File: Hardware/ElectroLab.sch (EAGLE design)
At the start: 244 parts, among them IC1 LM2902DT, IC10 CD4511BNSR, IC11 PAM8403, IC12 LM2902DT, IC13 ADXL337, IC14 MIC5205, IC2 LM2902DT, IC3 SN74LV08ADR, IC4 SN74LV32ADR, IC5 SN74LV04ADR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

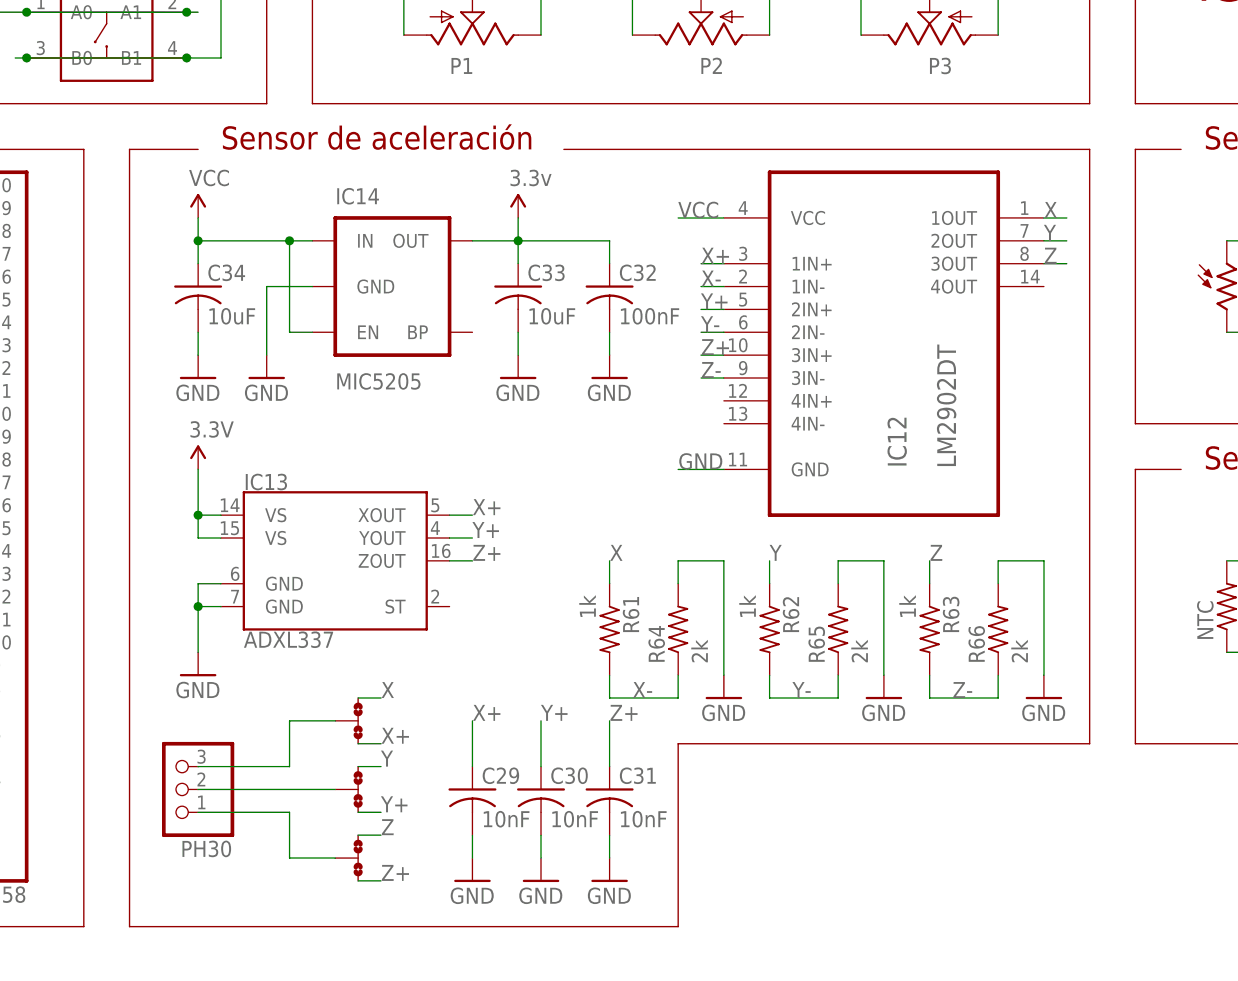
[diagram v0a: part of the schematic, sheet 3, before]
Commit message: Removed Amplifier after Acc ADXL337
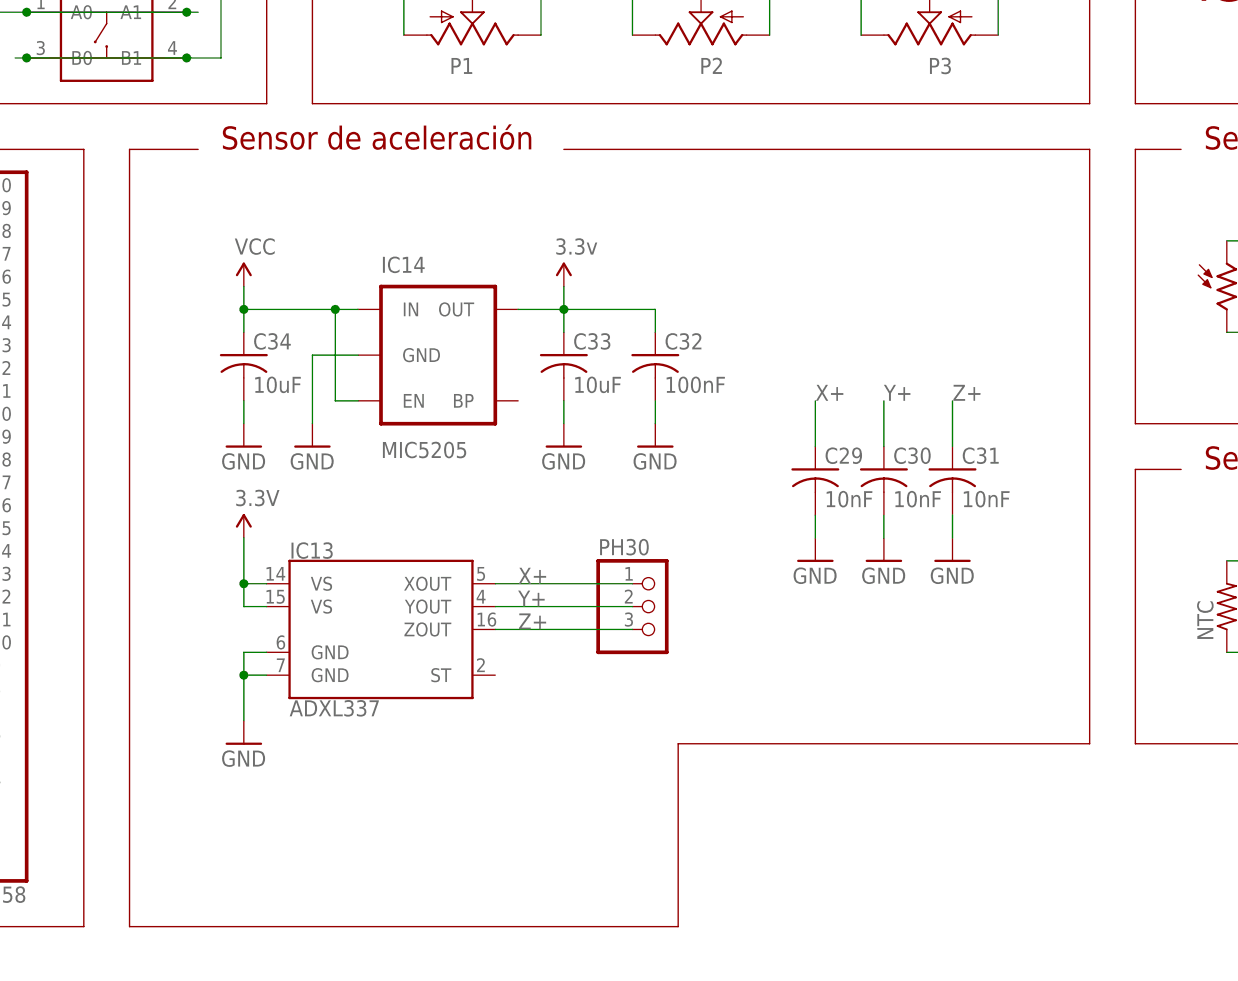
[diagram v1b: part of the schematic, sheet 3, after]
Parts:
- removed IC12: LM2902DT, Texas Instruments_By_element14_Batch_1:LM2902DT
- removed JMP7, JMP8, JMP9: 0R-JUMPA, jump-0r-smd:0R-JUMPA
- removed R61, R62, R63: 1k, SpaceDIY_passive_components:R0603
- removed R64, R65, R66: 2k, SpaceDIY_passive_components:R0603
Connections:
- removed net N$124: JMP8-0R.2, PH30.2
- removed net N$127: JMP7-0R.2, PH30.3
- removed net N$128: JMP9-0R.2, PH30.1
- removed net X: IC12.1OUT, JMP7-0R.3, R61.1
- removed net X-: IC12.1IN-, R61.2, R64.1
- removed net Y: IC12.2OUT, JMP8-0R.3, R62.1
- removed net Y-: IC12.2IN-, R62.2, R65.1
- removed net Z: IC12.3OUT, JMP9-0R.3, R63.1
- removed net Z-: IC12.3IN-, R63.2, R66.1
- net GND: no longer IC12.GND, R64.2, R65.2, R66.2
- net VCC: no longer IC12.VCC
- net X+: now also PH30.1; no longer IC12.1IN+, JMP7-0R.1
- net Y+: now also PH30.2; no longer IC12.2IN+, JMP8-0R.1
- net Z+: now also PH30.3; no longer IC12.3IN+, JMP9-0R.1
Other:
- moved on the sheet: C29, C30, C31, C32, C33, C34, IC13, IC14, PH30

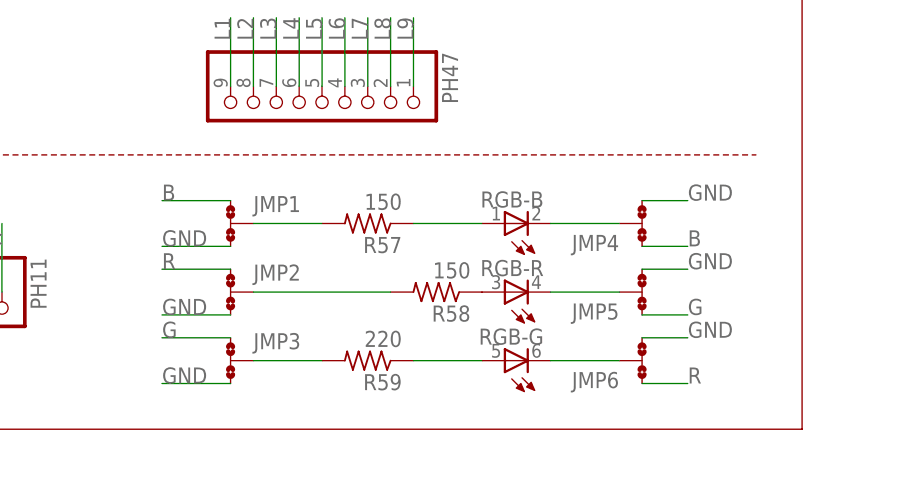
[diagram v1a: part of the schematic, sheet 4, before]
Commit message: Updated RGB layout
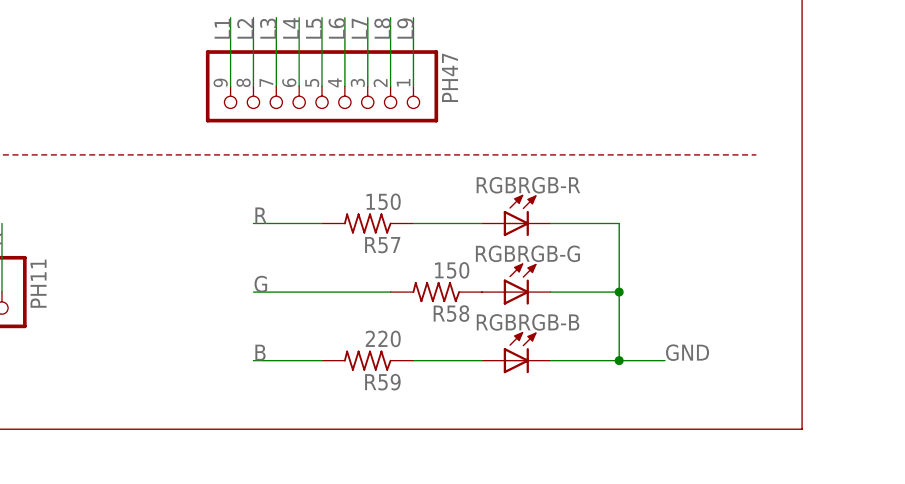
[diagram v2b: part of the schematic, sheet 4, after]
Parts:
- removed JMP1, JMP2, JMP3, JMP4, JMP5, JMP6: 0R-JUMPA, jump-0r-smd:0R-JUMPA
- RGB: value OVSTRGBBCR8 -> LED_RGB_PLCC6; device led:OVSTRGBBCR8 -> Passive_components:LED_RGB_PLCC6
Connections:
- removed net N$118: JMP2.2, R58.2
- removed net N$119: JMP3.2, R59.2
- removed net N$120: JMP4.2, RGB-B.C
- removed net N$121: JMP5.2, RGB-R.C
- removed net N$122: JMP6.2, RGB-G.C
- removed net N$309: R58.1, RGB-R.A
- net B: now also R59.2; no longer JMP1.1, JMP4.1
- net G: now also R58.2; no longer JMP3.1, JMP5.1
- net GND: now also RGBRGB-B.C, RGBRGB-G.C, RGBRGB-R.C; no longer JMP1.3, JMP2.3, JMP3.3, JMP4.3, JMP5.3, JMP6.3
- net N$117: now also R58.1, RGBRGB-G.A; no longer JMP1.2, R57.2
- net N$308: now also RGBRGB-R.A; no longer RGB-B.A
- net N$310: now also RGBRGB-B.A; no longer RGB-G.A
- net R: now also R57.2; no longer JMP2.1, JMP6.1

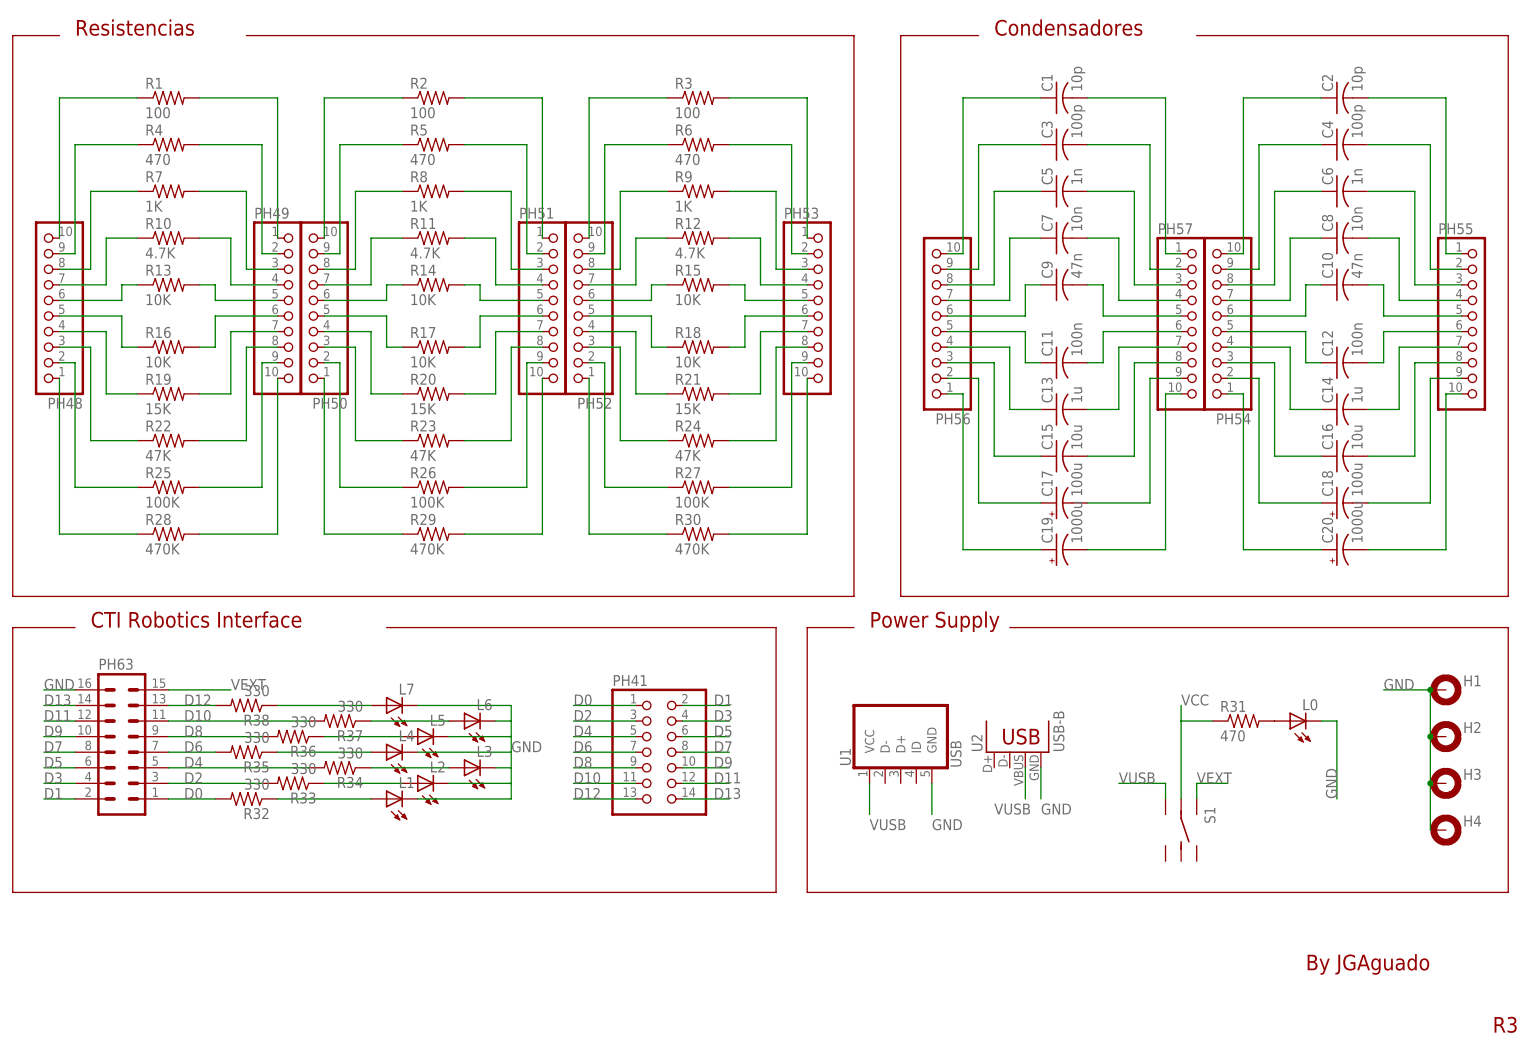
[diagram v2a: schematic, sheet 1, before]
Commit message: Capacitor area update: - Replaced C19 & C20 for 470uF 7343 (2917) Tantalum capacitors - Added C35 & C36 470uF 7343 (2917) in paralel to C19 & C20 for making 940uF combined - Reviewed Name and Values silkscreen for capacitors
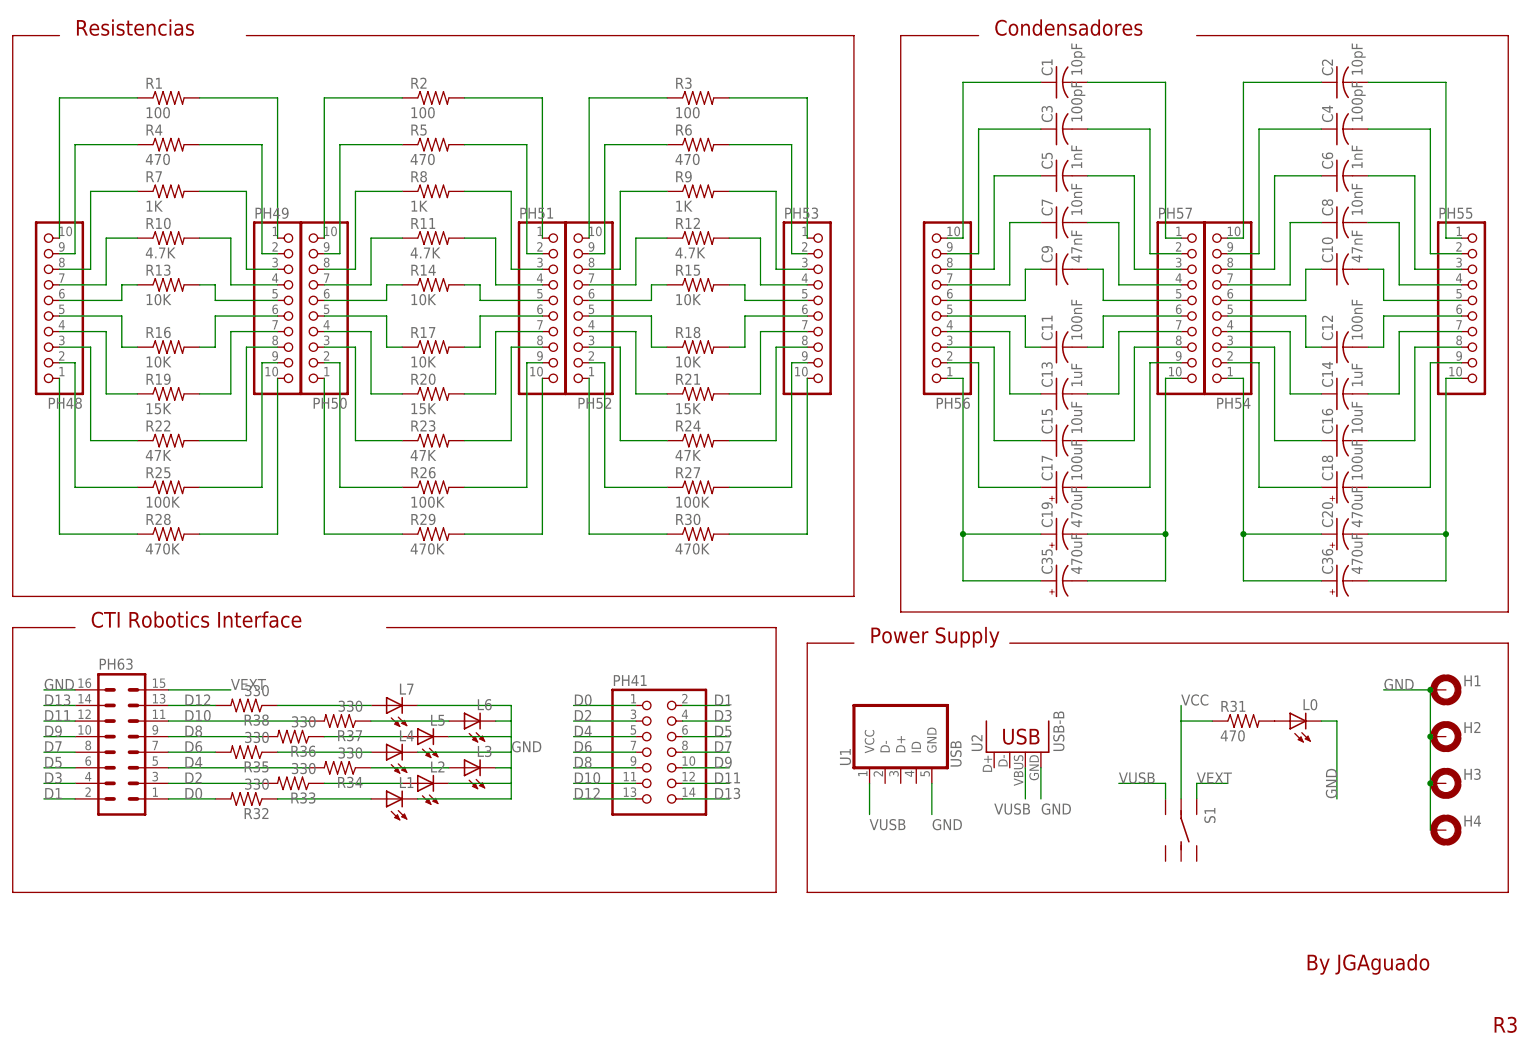
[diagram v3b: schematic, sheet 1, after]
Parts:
- added C35, C36: 470uF, rcl:CPOL-USD/7343-31R
- C1, C2: value 10p -> 10pF
- C10, C9: value 47n -> 47nF
- C11, C12: value 100n -> 100nF
- C13, C14: value 1u -> 1uF
- C15, C16: value 10u -> 10uF
- C17, C18: value 100u -> 100uF; device rcl:CPOL-USA/3216-18W -> rcl:CPOL-USA/3216-18R
- C19, C20: value 1000u -> 470uF; device rcl:CPOL-USD/7343-31W -> rcl:CPOL-USD/7343-31R
- C3, C4: value 100p -> 100pF
- C5, C6: value 1n -> 1nF
- C7, C8: value 10n -> 10nF
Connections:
- net N$70: now also C35.+
- net N$80: now also C35.-
- net N$90: now also C36.+
- net N$91: now also C36.-
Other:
- moved on the sheet: C1, C10, C11, C12, C13, C14, C15, C16, C17, C18, C19, C2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

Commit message: Update modifications for ElectroLab R2 CTI20 Release
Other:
- note added: "R2"
- note removed: "R3"
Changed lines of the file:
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@@
 <?xml version="1.0" encoding="utf-8"?>
 <!DOCTYPE eagle SYSTEM "eagle.dtd">
-<eagle version="9.4.2">
+<eagle version="9.5.1">
 <drawing>
 <settings>
@@
 <plain>
 <text x="218.44" y="15.24" size="2.54" layer="94">By JGAguado</text>
-<text x="248.92" y="5.08" size="2.54" layer="94">R3</text>
+<text x="248.92" y="5.08" size="2.54" layer="94">R2</text>
 <wire x1="152.4" y1="167.64" x2="152.4" y2="73.66" width="0.1524" layer="94"/>
 <wire x1="152.4" y1="73.66" x2="251.46" y2="73.66" width="0.1524" layer="94"/>
@@
 <wire x1="106.68" y1="10.16" x2="106.68" y2="33.02" width="0.1524" layer="94"/>
 <text x="218.44" y="15.24" size="2.54" layer="94">By JGAguado</text>
-<text x="248.92" y="5.08" size="2.54" layer="94">R3</text>
+<text x="248.92" y="5.08" size="2.54" layer="94">R2</text>
 </plain>
 <instances>
@@
 <wire x1="88.9" y1="7.62" x2="10.16" y2="7.62" width="0.1524" layer="94"/>
 <text x="218.44" y="15.24" size="2.54" layer="94">By JGAguado</text>
-<text x="248.92" y="5.08" size="2.54" layer="94">R3</text>
+<text x="248.92" y="5.08" size="2.54" layer="94">R2</text>
 </plain>
 <instances>
@@
 <wire x1="17.78" y1="38.1" x2="114.3" y2="38.1" width="0.1524" layer="94" style="longdash"/>
 <text x="218.44" y="15.24" size="2.54" layer="94">By JGAguado</text>
-<text x="248.92" y="5.08" size="2.54" layer="94">R3</text>
+<text x="248.92" y="5.08" size="2.54" layer="94">R2</text>
 </plain>
 <instances>
